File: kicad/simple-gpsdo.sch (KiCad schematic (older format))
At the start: 93 parts, among them J2 PWR, J3 ISP, J4 GPS_NEO, J5 GPS_IN, J6 10MHz_OUT, J7 NEO-6M, J8 10MHz_OUT, J9 USB_C_Receptacle_USB2.0, SW1 RST, U1 BD50FC0FP-E2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

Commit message: finalizing PCB, added 3D models
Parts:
- L2: footprint Inductor_SMD:L_1206_3216Metric_Pad1.42x1.75mm_HandSolder -> Inductor_SMD:L_Taiyo-Yuden_NR-50xx_HandSoldering
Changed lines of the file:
@@
 F 0 "L2" V 3450 6450 50  0000 L CNN
 F 1 "3.3uH" V 3350 6400 40  0000 L CNN
-F 2 "Inductor_SMD:L_1206_3216Metric_Pad1.42x1.75mm_HandSolder" H 3400 6500 50  0001 C CNN
+F 2 "Inductor_SMD:L_Taiyo-Yuden_NR-50xx_HandSoldering" H 3400 6500 50  0001 C CNN
 F 3 "~" H 3400 6500 50  0001 C CNN
 	1    3400 6500

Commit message: finalizing schematic
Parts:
- J9: value USB_C_Receptacle_USB2.0 -> USB_C
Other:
- note added: "12V -> 6V Buck Regulator\nKeeps Pdiss on the Linears Low"
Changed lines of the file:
@@
 P 1300 3100
 F 0 "J9" H 1407 3967 50  0000 C CNN
-F 1 "USB_C_Receptacle_USB2.0" H 1407 3876 50  0000 C CNN
+F 1 "USB_C" H 1407 3876 50  0000 C CNN
 F 2 "Kycon:KUSBX-SL-CS1N14-B" H 1450 3100 50  0001 C CNN
 F 3 "https://www.usb.org/sites/default/files/documents/usb_type-c.zip" H 1450 3100 50  0001 C CNN
@@
 Connection ~ 3600 6500
 Connection ~ 3900 6500
+Text Notes 1950 7300 0    50   ~ 0
+12V -> 6V Buck Regulator\nKeeps Pdiss on the Linears Low
 $EndSCHEMATC

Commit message: initial work on schematic updates
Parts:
- added C?: 10uF, Capacitor_SMD:C_1206_3216Metric_Pad1.42x1.75mm_HandSolder, symbol Device:CP_Small
- added L?: 3.3uH, Inductor_SMD:L_Taiyo-Yuden_NR-50xx_HandSoldering, symbol Device:L_Small
- L1: value 33uH -> 3.3uH
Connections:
- net GND: now also C?.2
- net at C28.2, C29.2, U1.1 (IN)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: now also C?.1, L?.2; no longer C27.1, C8.1, L2.2, R27.2
- new net: C27.1, C8.1, L2.2, L?.1, R27.2
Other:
- note added: ""Analog" Supply \nfor OCXO and\nLogic Gates"
- note added: ""Digital" supply\nfor ATMega and \nGPS"
- note added: "Extra filtering on 6V line"
- note removed: ""Analog" Supply for\nOCXO and Logic Gates"
- note removed: ""Digital" supply for\nATMega and GPS"
- moved on the sheet: C28, C29, C30, C31, U1, U5

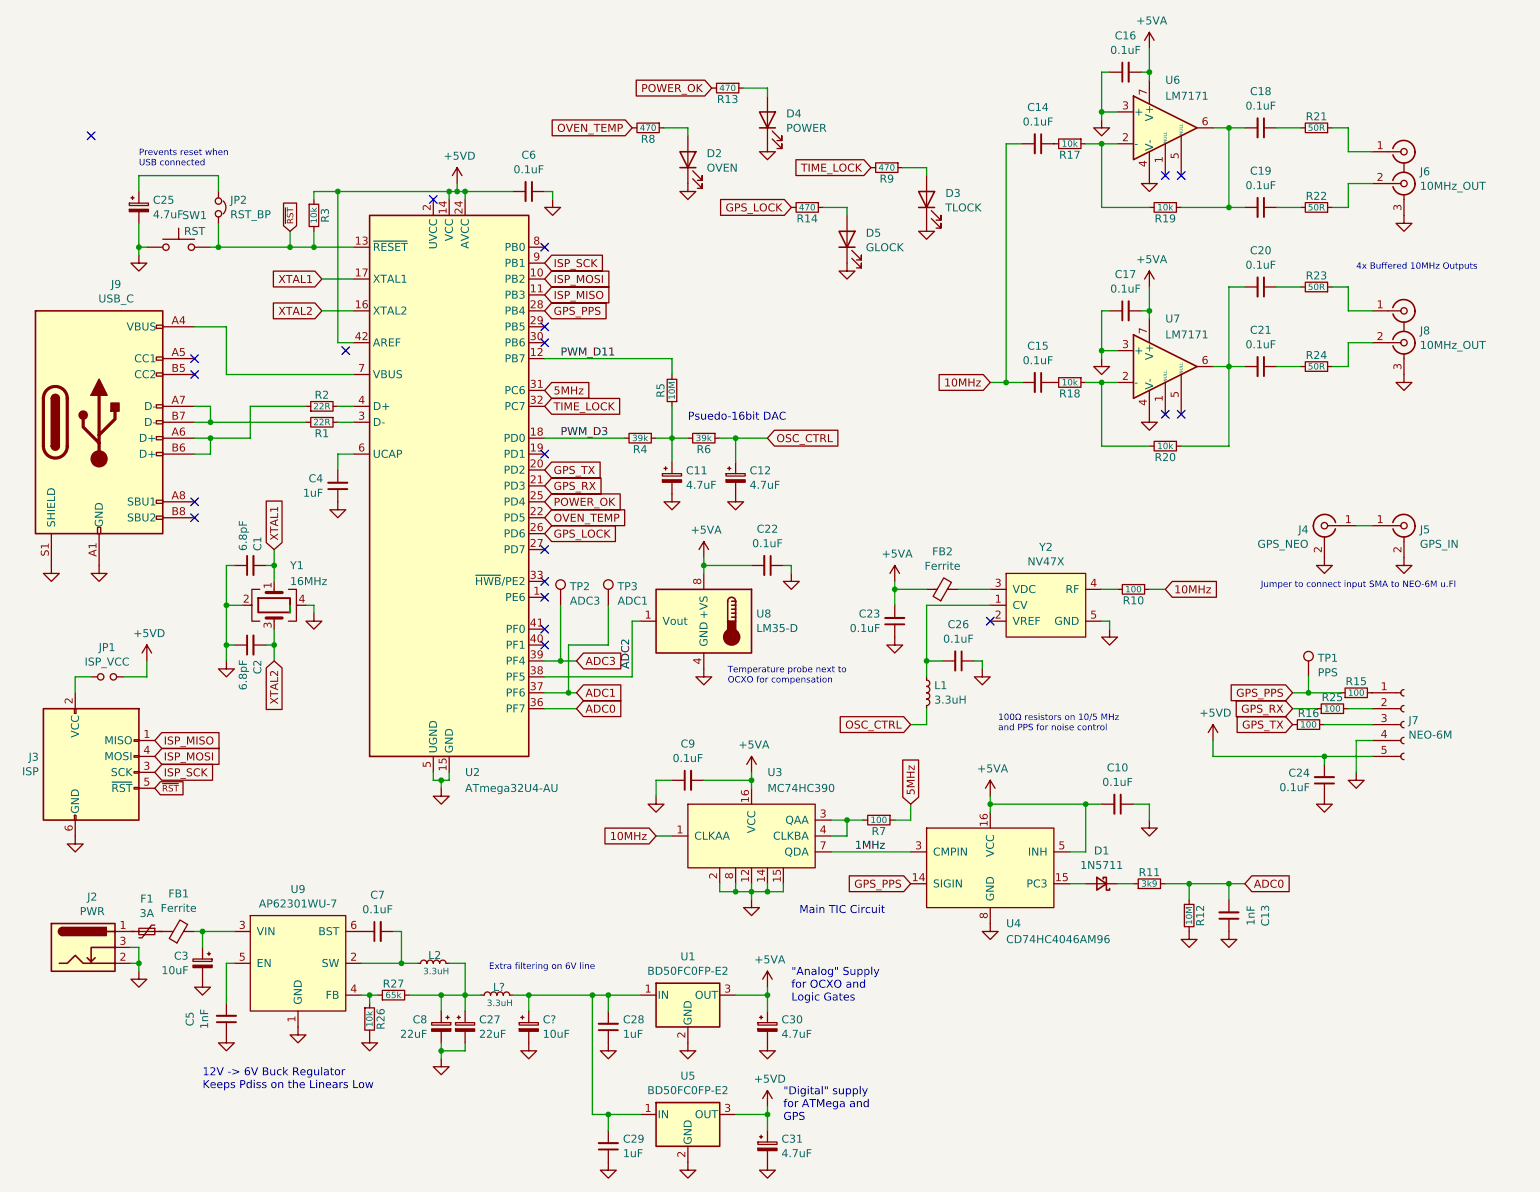
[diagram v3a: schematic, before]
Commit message: added extra buck filtering
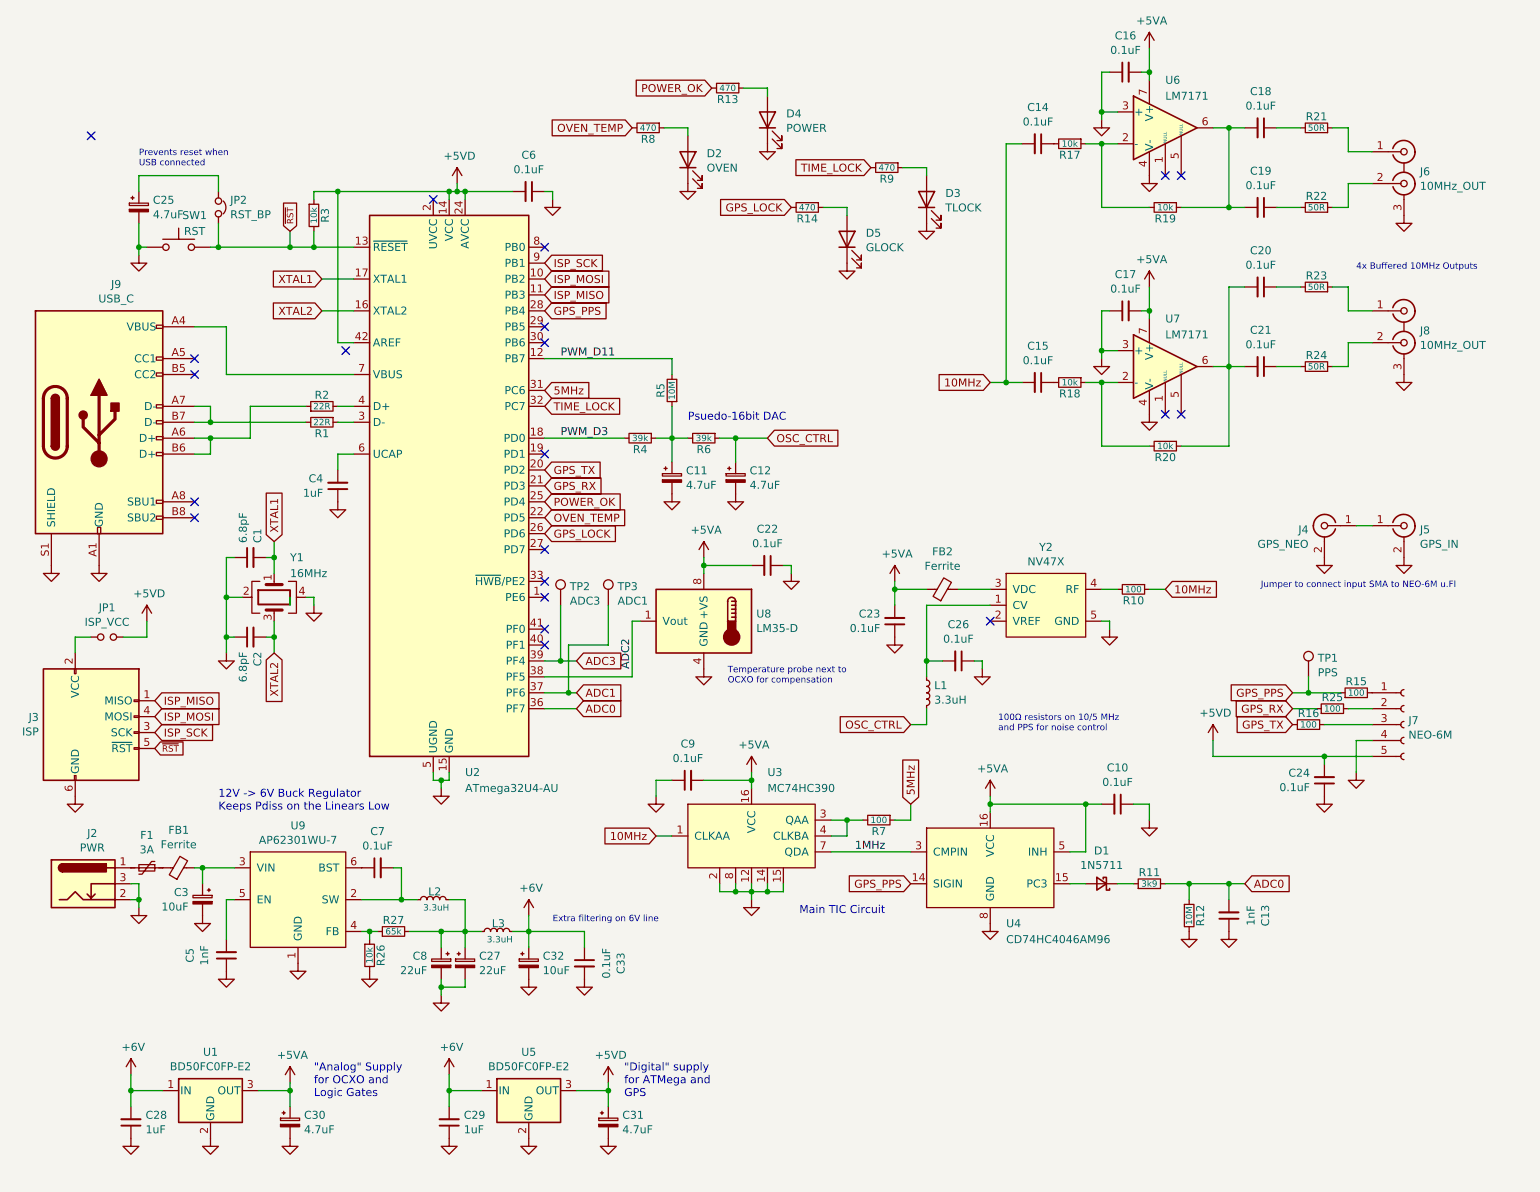
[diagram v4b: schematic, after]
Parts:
- added C33: 0.1uF, Capacitor_SMD:C_0805_2012Metric_Pad1.15x1.40mm_HandSolder, symbol Device:C_Small
- gave numbers to parts that had none: 2
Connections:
- net GND: now also C33.2
- net +6V: now reaches C28.2, C29.2, C32.1, L3.2, U1.1 (IN), U5.1 (IN)
- net +6V: now also C33.1
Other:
- moved on the sheet: C1, C2, C27, C28, C29, C3, C30, C31, C32, C5, C7, C8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

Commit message: finalizing revC schematic and board
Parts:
- added J1: PPS_OUT, Connector_PinHeader_2.54mm:PinHeader_2x01_P2.54mm_Vertical, symbol Connector:Conn_Coaxial
- added Q1: DMP3099L, Package_TO_SOT_SMD:SOT-23_Handsoldering, symbol Device:Q_PMOS_GSD
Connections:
- net GND: now also J1.2 (Ext), Q1.1 (G)
- net GPS_PPS: now also J1.1 (In)
- net at C3.1, U9.3 (VIN): now also Q1.2 (S); no longer FB1.2
- new net: FB1.2, Q1.3 (D)
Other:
- note added: "Reverse polarity NFET"
- moved on the sheet: C1, C10, C11, C12, C13, C2, C22, C23, C24, C25, C26, C27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

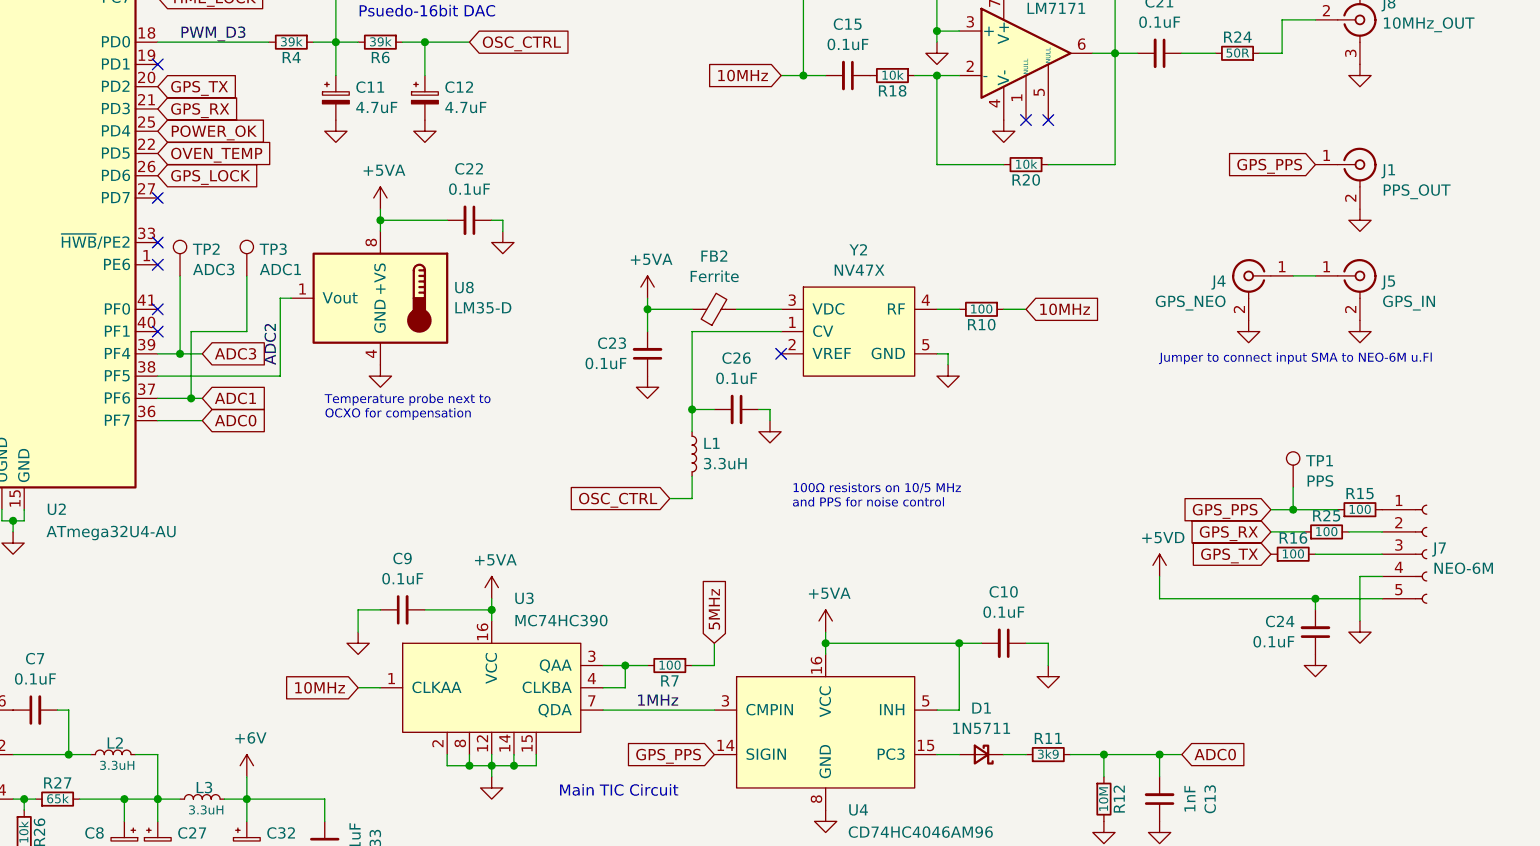
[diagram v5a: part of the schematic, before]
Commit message: added resistor/cap to NEO power in sch
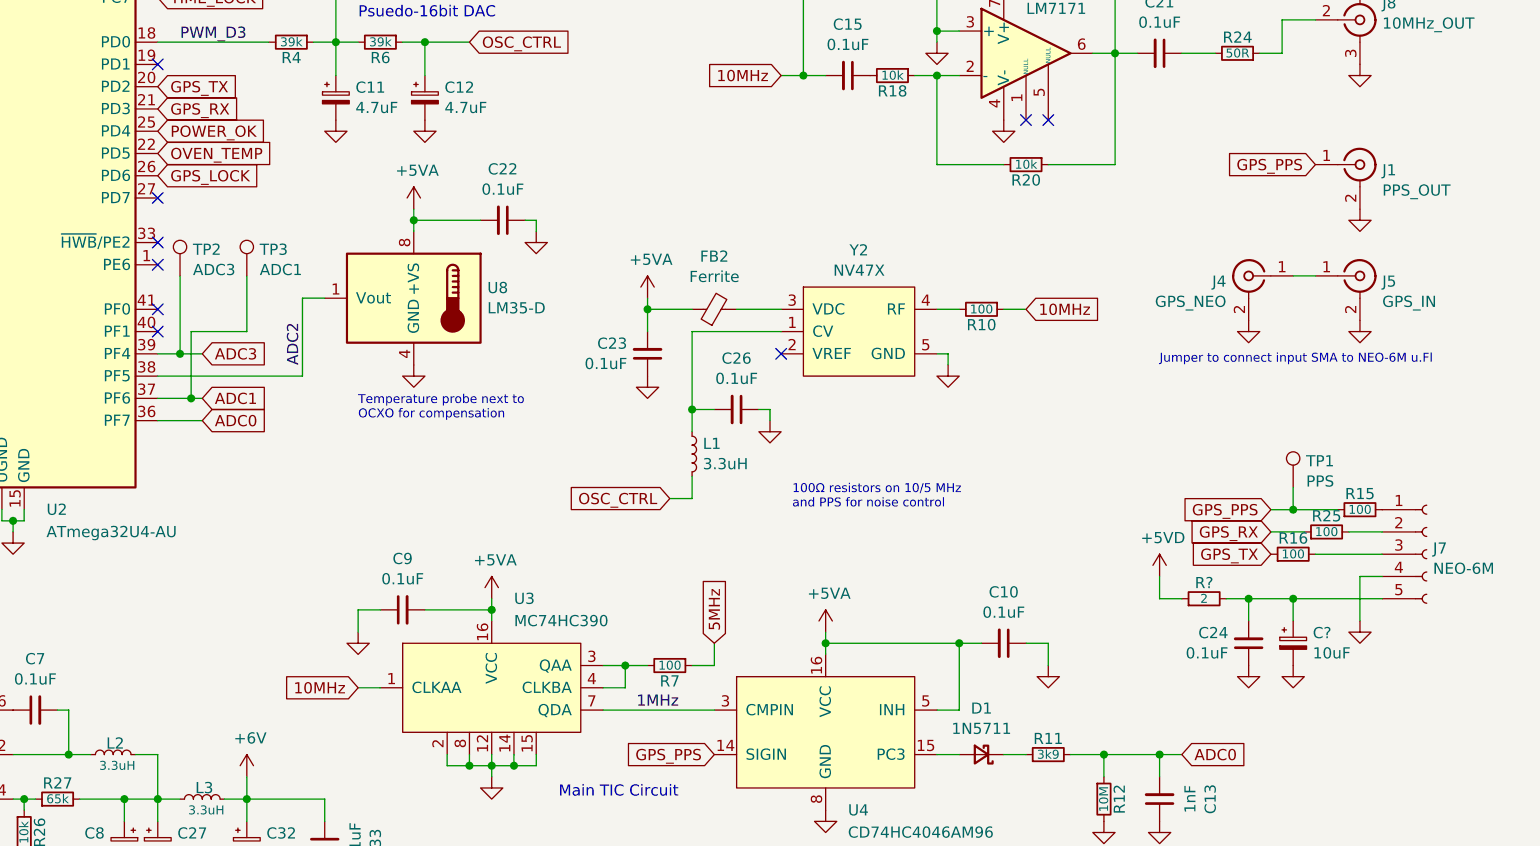
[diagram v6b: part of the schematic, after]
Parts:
- added C?: 10uF, Capacitor_SMD:C_1206_3216Metric_Pad1.42x1.75mm_HandSolder, symbol Device:CP_Small
- added R?: 2, Resistor_SMD:R_0805_2012Metric_Pad1.15x1.40mm_HandSolder, symbol Device:R_Small
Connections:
- net +5VD: now also R?.1; no longer C24.2, J7.5 (Pin_5)
- net GND: now also C?.2
- new net: C24.2, C?.1, J7.5 (Pin_5), R?.2
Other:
- moved on the sheet: C22, C24, U8
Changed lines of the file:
@@
 Text Notes 5000 2600 0    50   ~ 0
 Psuedo-16bit DAC
-Wire Wire Line
-	9300 5200 9600 5200
-Connection ~ 9300 5200
-Wire Wire Line
-	9300 5250 9300 5200
 $Comp
 L power:+5VD #PWR054
@@
 L power:GND #PWR055
 U 1 1 5F7B60F6
-P 9300 5450
-F 0 "#PWR055" H 9300 5200 50  0001 C CNN
-F 1 "GND" H 9305 5277 50  0001 C CNN
-F 2 "" H 9300 5450 50  0001 C CNN
-F 3 "" H 9300 5450 50  0001 C CNN
-	1    9300 5450
+P 9000 5500
+F 0 "#PWR055" H 9000 5250 50  0001 C CNN
+F 1 "GND" H 9005 5327 50  0001 C CNN
+F 2 "" H 9000 5500 50  0001 C CNN
+F 3 "" H 9000 5500 50  0001 C CNN
+	1    9000 5500
 	1    0    0    -1
 $EndComp
@@
 Text Label 4200 2200 0    50   ~ 0
 PWM_D11
-$Comp
-L Sensor_Temperature:LM35-D U8
-U 1 1 5FC5ED28
-P 5100 3850
-F 0 "U8" H 4770 3896 50  0000 R CNN
-F 1 "LM35-D" H 4770 3805 50  0000 R CNN
-F 2 "Package_SO:SOIC-8_3.9x4.9mm_P1.27mm" H 5100 3450 50  0001 C CNN
-F 3 "http://www.ti.com/lit/ds/symlink/lm35.pdf" H 5100 3850 50  0001 C CNN
-	1    5100 3850
-	-1   0    0    -1
-$EndComp
-$Comp
-L power:GND #PWR030
-U 1 1 5FC7A3C8
-P 5100 4150
-F 0 "#PWR030" H 5100 3900 50  0001 C CNN
-F 1 "GND" H 5105 3977 50  0001 C CNN
-F 2 "" H 5100 4150 50  0001 C CNN
-F 3 "" H 5100 4150 50  0001 C CNN
-	1    5100 4150
-	1    0    0    -1
-$EndComp
-$Comp
-L power:+5VA #PWR028
-U 1 1 5FC7A9C6
-P 5100 3450
-F 0 "#PWR028" H 5100 3300 50  0001 C CNN
-F 1 "+5VA" H 5115 3623 50  0000 C CNN
-F 2 "" H 5100 3450 50  0001 C CNN
-F 3 "" H 5100 3450 50  0001 C CNN
-	1    5100 3450
-	1    0    0    -1
-$EndComp
-$Comp
-L Device:C_Small C22
-U 1 1 5FC9842D
-P 5500 3500
-F 0 "C22" V 5271 3500 50  0000 C CNN
-F 1 "0.1uF" V 5362 3500 50  0000 C CNN
-F 2 "Capacitor_SMD:C_0805_2012Metric_Pad1.15x1.40mm_HandSolder" H 5500 3500 50  0001 C CNN
-F 3 "~" H 5500 3500 50  0001 C CNN
-	1    5500 3500
-	0    1    1    0
-$EndComp
-$Comp
-L power:GND #PWR038
-U 1 1 5FC993EA
-P 5650 3550
-F 0 "#PWR038" H 5650 3300 50  0001 C CNN
-F 1 "GND" H 5655 3377 50  0001 C CNN
-F 2 "" H 5650 3550 50  0001 C CNN
-F 3 "" H 5650 3550 50  0001 C CNN
-	1    5650 3550
-	1    0    0    -1
-$EndComp
-Wire Wire Line
-	5600 3500 5650 3500
-Wire Wire Line
-	5650 3500 5650 3550
-Wire Wire Line
-	5100 3450 5100 3500
-Wire Wire Line
-	5400 3500 5100 3500
-Connection ~ 5100 3500
-Wire Wire Line
-	5100 3500 5100 3550
-Wire Wire Line
-	4700 3850 4650 3850
-Wire Wire Line
-	4650 3850 4650 4200
-Text Notes 4850 4400 0    40   ~ 0
-Temperature probe next to\nOCXO for compensation
 NoConn ~ 4100 2000
 NoConn ~ 4100 3400
@@
 Text GLabel 4300 4300 2    50   Input ~ 0
 ADC1
-Text Label 4650 4150 1    50   ~ 0
-ADC2
 $Comp
 L Bliley:NV47X Y2
@@
 $EndComp
 NoConn ~ 6900 4100
-Wire Wire Line
-	4100 4200 4650 4200
 Wire Wire Line
 	4100 4300 4250 4300
@@
 	8600 5200 8600 5100
 Wire Wire Line
-	8600 5200 9300 5200
-Wire Wire Line
 	6900 4000 6500 4000
 Wire Wire Line
@@
 L Device:C_Small C24
 U 1 1 5F7B60EC
-P 9300 5350
-F 0 "C24" H 9209 5304 50  0000 R CNN
-F 1 "0.1uF" H 9209 5395 50  0000 R CNN
-F 2 "Capacitor_SMD:C_0805_2012Metric_Pad1.15x1.40mm_HandSolder" H 9300 5350 50  0001 C CNN
-F 3 "~" H 9300 5350 50  0001 C CNN
-	1    9300 5350
+P 9000 5400
+F 0 "C24" H 8909 5354 50  0000 R CNN
+F 1 "0.1uF" H 8909 5445 50  0000 R CNN
+F 2 "Capacitor_SMD:C_0805_2012Metric_Pad1.15x1.40mm_HandSolder" H 9000 5400 50  0001 C CNN
+F 3 "~" H 9000 5400 50  0001 C CNN
+	1    9000 5400
 	1    0    0    1
 $EndComp
@@
 Text GLabel 9300 3250 0    50   Input ~ 0
 GPS_PPS
+Text Label 4750 4150 1    50   ~ 0
+ADC2
+Text Notes 5000 4400 0    40   ~ 0
+Temperature probe next to\nOCXO for compensation
+Wire Wire Line
+	5250 3500 5250 3550
+Connection ~ 5250 3500
+Wire Wire Line
+	5550 3500 5250 3500
+Wire Wire Line
+	5250 3450 5250 3500
+Wire Wire Line
+	5800 3500 5800 3550
+Wire Wire Line
+	5750 3500 5800 3500
+$Comp
+L power:GND #PWR038
+U 1 1 5FC993EA
+P 5800 3550
+F 0 "#PWR038" H 5800 3300 50  0001 C CNN
+F 1 "GND" H 5805 3377 50  0001 C CNN
+F 2 "" H 5800 3550 50  0001 C CNN
+F 3 "" H 5800 3550 50  0001 C CNN
+	1    5800 3550
+	1    0    0    -1
+$EndComp
+$Comp
+L Device:C_Small C22
+U 1 1 5FC9842D
+P 5650 3500
+F 0 "C22" V 5421 3500 50  0000 C CNN
+F 1 "0.1uF" V 5512 3500 50  0000 C CNN
+F 2 "Capacitor_SMD:C_0805_2012Metric_Pad1.15x1.40mm_HandSolder" H 5650 3500 50  0001 C CNN
+F 3 "~" H 5650 3500 50  0001 C CNN
+	1    5650 3500
+	0    1    1    0
+$EndComp
+$Comp
+L power:+5VA #PWR028
+U 1 1 5FC7A9C6
+P 5250 3450
+F 0 "#PWR028" H 5250 3300 50  0001 C CNN
+F 1 "+5VA" H 5265 3623 50  0000 C CNN
+F 2 "" H 5250 3450 50  0001 C CNN
+F 3 "" H 5250 3450 50  0001 C CNN
+	1    5250 3450
+	1    0    0    -1
+$EndComp
+$Comp
+L power:GND #PWR030
+U 1 1 5FC7A3C8
+P 5250 4150
+F 0 "#PWR030" H 5250 3900 50  0001 C CNN
+F 1 "GND" H 5255 3977 50  0001 C CNN
+F 2 "" H 5250 4150 50  0001 C CNN
+F 3 "" H 5250 4150 50  0001 C CNN
+	1    5250 4150
+	1    0    0    -1
+$EndComp
+$Comp
+L Sensor_Temperature:LM35-D U8
+U 1 1 5FC5ED28
+P 5250 3850
+F 0 "U8" H 4920 3896 50  0000 R CNN
+F 1 "LM35-D" H 4920 3805 50  0000 R CNN
+F 2 "Package_SO:SOIC-8_3.9x4.9mm_P1.27mm" H 5250 3450 50  0001 C CNN
+F 3 "http://www.ti.com/lit/ds/symlink/lm35.pdf" H 5250 3850 50  0001 C CNN
+	1    5250 3850
+	-1   0    0    -1
+$EndComp
+Wire Wire Line
+	4750 3850 4750 4200
+Wire Wire Line
+	4750 3850 4850 3850
+Wire Wire Line
+	4100 4200 4750 4200
+$Comp
+L Device:CP_Small C?
+U 1 1 5F8452F2
+P 9200 5400
+F 0 "C?" H 9288 5446 50  0000 L CNN
+F 1 "10uF" H 9288 5355 50  0000 L CNN
+F 2 "Capacitor_SMD:C_1206_3216Metric_Pad1.42x1.75mm_HandSolder" H 9200 5400 50  0001 C CNN
+F 3 "~" H 9200 5400 50  0001 C CNN
+	1    9200 5400
+	1    0    0    -1
+$EndComp
+$Comp
+L power:GND #PWR?
+U 1 1 5F88788D
+P 9200 5500
+F 0 "#PWR?" H 9200 5250 50  0001 C CNN
+F 1 "GND" H 9205 5327 50  0001 C CNN
+F 2 "" H 9200 5500 50  0001 C CNN
+F 3 "" H 9200 5500 50  0001 C CNN
+	1    9200 5500
+	1    0    0    -1
+$EndComp
+Wire Wire Line
+	9000 5200 9000 5300
+Wire Wire Line
+	9200 5300 9200 5200
+Connection ~ 9200 5200
+Wire Wire Line
+	9200 5200 9600 5200
+Wire Wire Line
+	9000 5200 9200 5200
+$Comp
+L Device:R_Small R?
+U 1 1 5F8F0055
+P 8800 5200
+F 0 "R?" V 8900 5200 50  0000 C BNN
+F 1 "2" V 8800 5200 40  0000 C CNN
+F 2 "Resistor_SMD:R_0805_2012Metric_Pad1.15x1.40mm_HandSolder" H 8800 5200 50  0001 C CNN
+F 3 "~" H 8800 5200 50  0001 C CNN
+	1    8800 5200
+	0    -1   -1   0
+$EndComp
+Wire Wire Line
+	8600 5200 8700 5200
+Wire Wire Line
+	8900 5200 9000 5200
+Connection ~ 9000 5200
 $EndSCHEMATC
